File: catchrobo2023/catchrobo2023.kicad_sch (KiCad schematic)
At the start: 34 parts, among them J1 Conn_01x03_Male, J2 Conn_01x03_Male, J3 Conn_01x03_Male, J4 Conn_01x02_Male, J5 Conn_01x02_Male, J6 Conn_01x02_Male, J7 Conn_01x02_Male, J8 Conn_01x02_Male, Q1 AO3401A, SW1 SW_SPDT, SW2 SW_DIP_x04, U11 SPT15, U2 RaspberryPiPicoW, U3 AZ1084-5.0, U4 LBR-127HLD, U5 LBR-127HLD, U6 LBR-127HLD, U7 LBR-127HLD, U8 CD4051BM96

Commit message: 部品配置一旦終わり
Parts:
- U4, U5, U6, U7: footprint Connector_JST:JST_XH_B4B-XH-AM_1x04_P2.50mm_Vertical -> Connector_PinHeader_2.54mm:PinHeader_1x04_P2.54mm_Vertical
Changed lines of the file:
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@@
     (property "Reference" "U4" (id 0) (at 153.67 19.211 0))
     (property "Value" "LBR-127HLD" (id 1) (at 153.67 21.7479 0))
-    (property "Footprint" "Connector_JST:JST_XH_B4B-XH-AM_1x04_P2.50mm_Vertical" (id 2) (at 151.13 26.67 0)
+    (property "Footprint" "Connector_PinHeader_2.54mm:PinHeader_1x04_P2.54mm_Vertical" (id 2) (at 151.13 26.67 0)
       (effects (font (size 1.27 1.27)) hide)
     )
@@
     (property "Reference" "U7" (id 0) (at 153.67 80.171 0))
     (property "Value" "LBR-127HLD" (id 1) (at 153.67 82.7079 0))
-    (property "Footprint" "Connector_JST:JST_XH_B4B-XH-AM_1x04_P2.50mm_Vertical" (id 2) (at 151.13 87.63 0)
+    (property "Footprint" "Connector_PinHeader_2.54mm:PinHeader_1x04_P2.54mm_Vertical" (id 2) (at 151.13 87.63 0)
       (effects (font (size 1.27 1.27)) hide)
     )
@@
     (property "Reference" "U5" (id 0) (at 153.67 39.531 0))
     (property "Value" "LBR-127HLD" (id 1) (at 153.67 42.0679 0))
-    (property "Footprint" "Connector_JST:JST_XH_B4B-XH-AM_1x04_P2.50mm_Vertical" (id 2) (at 151.13 46.99 0)
+    (property "Footprint" "Connector_PinHeader_2.54mm:PinHeader_1x04_P2.54mm_Vertical" (id 2) (at 151.13 46.99 0)
       (effects (font (size 1.27 1.27)) hide)
     )
@@
     (property "Reference" "U6" (id 0) (at 153.67 59.851 0))
     (property "Value" "LBR-127HLD" (id 1) (at 153.67 62.3879 0))
-    (property "Footprint" "Connector_JST:JST_XH_B4B-XH-AM_1x04_P2.50mm_Vertical" (id 2) (at 151.13 67.31 0)
+    (property "Footprint" "Connector_PinHeader_2.54mm:PinHeader_1x04_P2.54mm_Vertical" (id 2) (at 151.13 67.31 0)
       (effects (font (size 1.27 1.27)) hide)
     )
@@
     )
     (path "/309bee41-de7c-4d48-85d7-c3c896b9413c"
-      (reference "U4") (unit 1) (value "LBR-127HLD") (footprint "Connector_JST:JST_XH_B4B-XH-AM_1x04_P2.50mm_Vertical")
+      (reference "U4") (unit 1) (value "LBR-127HLD") (footprint "Connector_PinHeader_2.54mm:PinHeader_1x04_P2.54mm_Vertical")
     )
     (path "/af13191f-f9fa-47db-8264-81b4e002b7be"
-      (reference "U5") (unit 1) (value "LBR-127HLD") (footprint "Connector_JST:JST_XH_B4B-XH-AM_1x04_P2.50mm_Vertical")
+      (reference "U5") (unit 1) (value "LBR-127HLD") (footprint "Connector_PinHeader_2.54mm:PinHeader_1x04_P2.54mm_Vertical")
     )
     (path "/c38467f7-e2c2-4708-991a-d2b698bca907"
-      (reference "U6") (unit 1) (value "LBR-127HLD") (footprint "Connector_JST:JST_XH_B4B-XH-AM_1x04_P2.50mm_Vertical")
+      (reference "U6") (unit 1) (value "LBR-127HLD") (footprint "Connector_PinHeader_2.54mm:PinHeader_1x04_P2.54mm_Vertical")
     )
     (path "/a7989e6a-60f8-412a-8d42-c272f1f8d212"
-      (reference "U7") (unit 1) (value "LBR-127HLD") (footprint "Connector_JST:JST_XH_B4B-XH-AM_1x04_P2.50mm_Vertical")
+      (reference "U7") (unit 1) (value "LBR-127HLD") (footprint "Connector_PinHeader_2.54mm:PinHeader_1x04_P2.54mm_Vertical")
     )
     (path "/319fb9ff-c20b-47c6-b5a0-e117048a4ec9"

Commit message: 部品配置完了！
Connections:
- net Sensor0: now also U8.15 (2); no longer U8.1 (4)
- net Sensor1: now also U8.14 (1); no longer U8.2 (6)
- net Sensor2: now also U8.13 (0); no longer U8.4 (7)
- net Sensor3: now also U8.12 (3); no longer U8.5 (8)
- net MultiC: no longer names the net of U8.9 (C)
- net MultiC: no longer U2.21 (GP16)
- no-connect marks 18 -> 20
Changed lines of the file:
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@@
   (no_connect (at 66.04 36.83))
   (no_connect (at 66.04 34.29))
-  (no_connect (at 165.1 106.68))
-  (no_connect (at 165.1 111.76))
-  (no_connect (at 165.1 109.22))
-  (no_connect (at 165.1 114.3))
   (no_connect (at 96.52 41.91))
   (no_connect (at 96.52 44.45))
   (no_connect (at 96.52 24.13))
+  (no_connect (at 96.52 69.85))
+  (no_connect (at 165.1 121.92))
+  (no_connect (at 147.32 114.3))
+  (no_connect (at 147.32 104.14))
+  (no_connect (at 147.32 106.68))
+  (no_connect (at 147.32 111.76))
   (no_connect (at 54.61 81.28))
   (no_connect (at 96.52 34.29))
@@
     (stroke (width 0) (type default) (color 0 0 0 0))
   )
-  (wire (pts (xy 165.1 121.92) (xy 168.91 121.92))
-    (stroke (width 0) (type default) (color 0 0 0 0))
-  )
   (wire (pts (xy 77.47 86.36) (xy 83.82 86.36))
     (stroke (width 0) (type default) (color 0 0 0 0))
@@
     (stroke (width 0) (type default) (color 0 0 0 0))
   )
-  (wire (pts (xy 143.51 104.14) (xy 147.32 104.14))
+  (wire (pts (xy 168.91 114.3) (xy 165.1 114.3))
     (stroke (width 0) (type default) (color 0 0 0 0))
   )
@@
     (stroke (width 0) (type default) (color 0 0 0 0))
   )
-  (wire (pts (xy 143.51 111.76) (xy 147.32 111.76))
+  (wire (pts (xy 168.91 109.22) (xy 165.1 109.22))
     (stroke (width 0) (type default) (color 0 0 0 0))
   )
@@
     (stroke (width 0) (type default) (color 0 0 0 0))
   )
-  (wire (pts (xy 96.52 69.85) (xy 101.6 69.85))
-    (stroke (width 0) (type default) (color 0 0 0 0))
-  )
   (wire (pts (xy 138.43 143.51) (xy 138.43 152.4))
     (stroke (width 0) (type default) (color 0 0 0 0))
@@
     (stroke (width 0) (type default) (color 0 0 0 0))
   )
-  (wire (pts (xy 143.51 106.68) (xy 147.32 106.68))
-    (stroke (width 0) (type default) (color 0 0 0 0))
-  )
-  (wire (pts (xy 143.51 114.3) (xy 147.32 114.3))
+  (wire (pts (xy 168.91 106.68) (xy 165.1 106.68))
+    (stroke (width 0) (type default) (color 0 0 0 0))
+  )
+  (wire (pts (xy 168.91 111.76) (xy 165.1 111.76))
     (stroke (width 0) (type default) (color 0 0 0 0))
   )
@@
     (effects (font (size 1.27 1.27)) (justify left bottom))
   )
-  (label "Sensor0" (at 143.51 104.14 180)
-    (effects (font (size 1.27 1.27)) (justify right bottom))
+  (label "Sensor3" (at 168.91 114.3 0)
+    (effects (font (size 1.27 1.27)) (justify left bottom))
   )
   (label "Servo2" (at 58.42 24.13 180)
     (effects (font (size 1.27 1.27)) (justify right bottom))
   )
-  (label "MultiC" (at 101.6 69.85 0)
-    (effects (font (size 1.27 1.27)) (justify left bottom))
-  )
   (label "DIPSW3" (at 104.14 54.61 0)
     (effects (font (size 1.27 1.27)) (justify left bottom))
   )
-  (label "Sensor3" (at 143.51 114.3 180)
-    (effects (font (size 1.27 1.27)) (justify right bottom))
+  (label "Sensor2" (at 168.91 111.76 0)
+    (effects (font (size 1.27 1.27)) (justify left bottom))
   )
   (label "Sensor2" (at 168.91 73.66 0)
     (effects (font (size 1.27 1.27)) (justify left bottom))
   )
-  (label "Sensor1" (at 143.51 106.68 180)
-    (effects (font (size 1.27 1.27)) (justify right bottom))
+  (label "Sensor0" (at 168.91 106.68 0)
+    (effects (font (size 1.27 1.27)) (justify left bottom))
   )
   (label "Servo2" (at 231.14 106.68 180)
@@
     (effects (font (size 1.27 1.27)) (justify right bottom))
   )
-  (label "Sensor2" (at 143.51 111.76 180)
-    (effects (font (size 1.27 1.27)) (justify right bottom))
+  (label "Sensor1" (at 168.91 109.22 0)
+    (effects (font (size 1.27 1.27)) (justify left bottom))
   )
   (label "DIPSW1" (at 78.74 146.05 0)
@@
     (effects (font (size 1.27 1.27)) (justify left bottom))
   )
-  (label "MultiC" (at 168.91 121.92 0)
-    (effects (font (size 1.27 1.27)) (justify left bottom))
-  )

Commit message: フォトリフレクタの周辺を修正
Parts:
- R10, R11, R2, R3, R4, R5: footprint Resistor_SMD:R_0201_0603Metric -> Resistor_SMD:R_0603_1608Metric
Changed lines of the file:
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@@
     (property "Reference" "R3" (id 0) (at 134.62 39.7342 90))
     (property "Value" "220" (id 1) (at 134.62 42.2711 90))
-    (property "Footprint" "Resistor_SMD:R_0201_0603Metric" (id 2) (at 134.62 46.228 90)
+    (property "Footprint" "Resistor_SMD:R_0603_1608Metric" (id 2) (at 134.62 46.228 90)
       (effects (font (size 1.27 1.27)) hide)
     )
@@
     (property "Reference" "R5" (id 0) (at 134.62 80.3742 90))
     (property "Value" "220" (id 1) (at 134.62 82.9111 90))
-    (property "Footprint" "Resistor_SMD:R_0201_0603Metric" (id 2) (at 134.62 86.868 90)
+    (property "Footprint" "Resistor_SMD:R_0603_1608Metric" (id 2) (at 134.62 86.868 90)
       (effects (font (size 1.27 1.27)) hide)
     )
@@
     (property "Reference" "R2" (id 0) (at 134.62 19.4142 90))
     (property "Value" "220" (id 1) (at 134.62 21.9511 90))
-    (property "Footprint" "Resistor_SMD:R_0201_0603Metric" (id 2) (at 134.62 25.908 90)
+    (property "Footprint" "Resistor_SMD:R_0603_1608Metric" (id 2) (at 134.62 25.908 90)
       (effects (font (size 1.27 1.27)) hide)
     )
@@
     (property "Reference" "R4" (id 0) (at 134.62 60.0542 90))
     (property "Value" "220" (id 1) (at 134.62 62.5911 90))
-    (property "Footprint" "Resistor_SMD:R_0201_0603Metric" (id 2) (at 134.62 66.548 90)
+    (property "Footprint" "Resistor_SMD:R_0603_1608Metric" (id 2) (at 134.62 66.548 90)
       (effects (font (size 1.27 1.27)) hide)
     )
@@
     (property "Reference" "R10" (id 0) (at 43.18 99.4242 90))
     (property "Value" "330" (id 1) (at 43.18 101.9611 90))
-    (property "Footprint" "Resistor_SMD:R_0201_0603Metric" (id 2) (at 43.18 105.918 90)
+    (property "Footprint" "Resistor_SMD:R_0603_1608Metric" (id 2) (at 43.18 105.918 90)
       (effects (font (size 1.27 1.27)) hide)
     )
@@
       (effects (font (size 1.27 1.27)) (justify left))
     )
-    (property "Footprint" "Resistor_SMD:R_0201_0603Metric" (id 2) (at 50.292 95.25 90)
+    (property "Footprint" "Resistor_SMD:R_0603_1608Metric" (id 2) (at 50.292 95.25 90)
       (effects (font (size 1.27 1.27)) hide)
     )
@@
     )
     (path "/4ece2eda-b20c-4e8f-ae6f-4d41de08f2b3"
-      (reference "R2") (unit 1) (value "220") (footprint "Resistor_SMD:R_0201_0603Metric")
+      (reference "R2") (unit 1) (value "220") (footprint "Resistor_SMD:R_0603_1608Metric")
     )
     (path "/485ce62a-bda4-46b8-b057-92a633eb73eb"
-      (reference "R3") (unit 1) (value "220") (footprint "Resistor_SMD:R_0201_0603Metric")
+      (reference "R3") (unit 1) (value "220") (footprint "Resistor_SMD:R_0603_1608Metric")
     )
     (path "/57897478-fc15-49af-a13c-0b635c80d981"
-      (reference "R4") (unit 1) (value "220") (footprint "Resistor_SMD:R_0201_0603Metric")
+      (reference "R4") (unit 1) (value "220") (footprint "Resistor_SMD:R_0603_1608Metric")
     )
     (path "/49080837-0b91-4e30-bf8a-b0058ad8b94b"
-      (reference "R5") (unit 1) (value "220") (footprint "Resistor_SMD:R_0201_0603Metric")
+      (reference "R5") (unit 1) (value "220") (footprint "Resistor_SMD:R_0603_1608Metric")
     )
     (path "/84754273-b66e-46a4-8959-627db908f4ff"
@@
     )
     (path "/5c226758-3cc0-45c8-83c2-343691c8c69e"
-      (reference "R10") (unit 1) (value "330") (footprint "Resistor_SMD:R_0201_0603Metric")
+      (reference "R10") (unit 1) (value "330") (footprint "Resistor_SMD:R_0603_1608Metric")
     )
     (path "/e09fb322-eccd-41fe-9289-f843fa181def"
-      (reference "R11") (unit 1) (value "10k") (footprint "Resistor_SMD:R_0201_0603Metric")
+      (reference "R11") (unit 1) (value "10k") (footprint "Resistor_SMD:R_0603_1608Metric")
     )
     (path "/f8c78e15-c342-4ab0-8f4b-67d61e7bd8ef"

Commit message: 製造ファイルまで出力
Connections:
- net Sensor0: now also U8.13 (0); no longer U8.15 (2)
- net Sensor2: now also U8.15 (2); no longer U8.13 (0)
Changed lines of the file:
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@@
     (effects (font (size 1.27 1.27)) (justify left bottom))
   )
-  (label "Sensor2" (at 168.91 111.76 0)
+  (label "Sensor0" (at 168.91 111.76 0)
     (effects (font (size 1.27 1.27)) (justify left bottom))
   )
@@
     (effects (font (size 1.27 1.27)) (justify left bottom))
   )
-  (label "Sensor0" (at 168.91 106.68 0)
+  (label "Sensor2" (at 168.91 106.68 0)
     (effects (font (size 1.27 1.27)) (justify left bottom))
   )

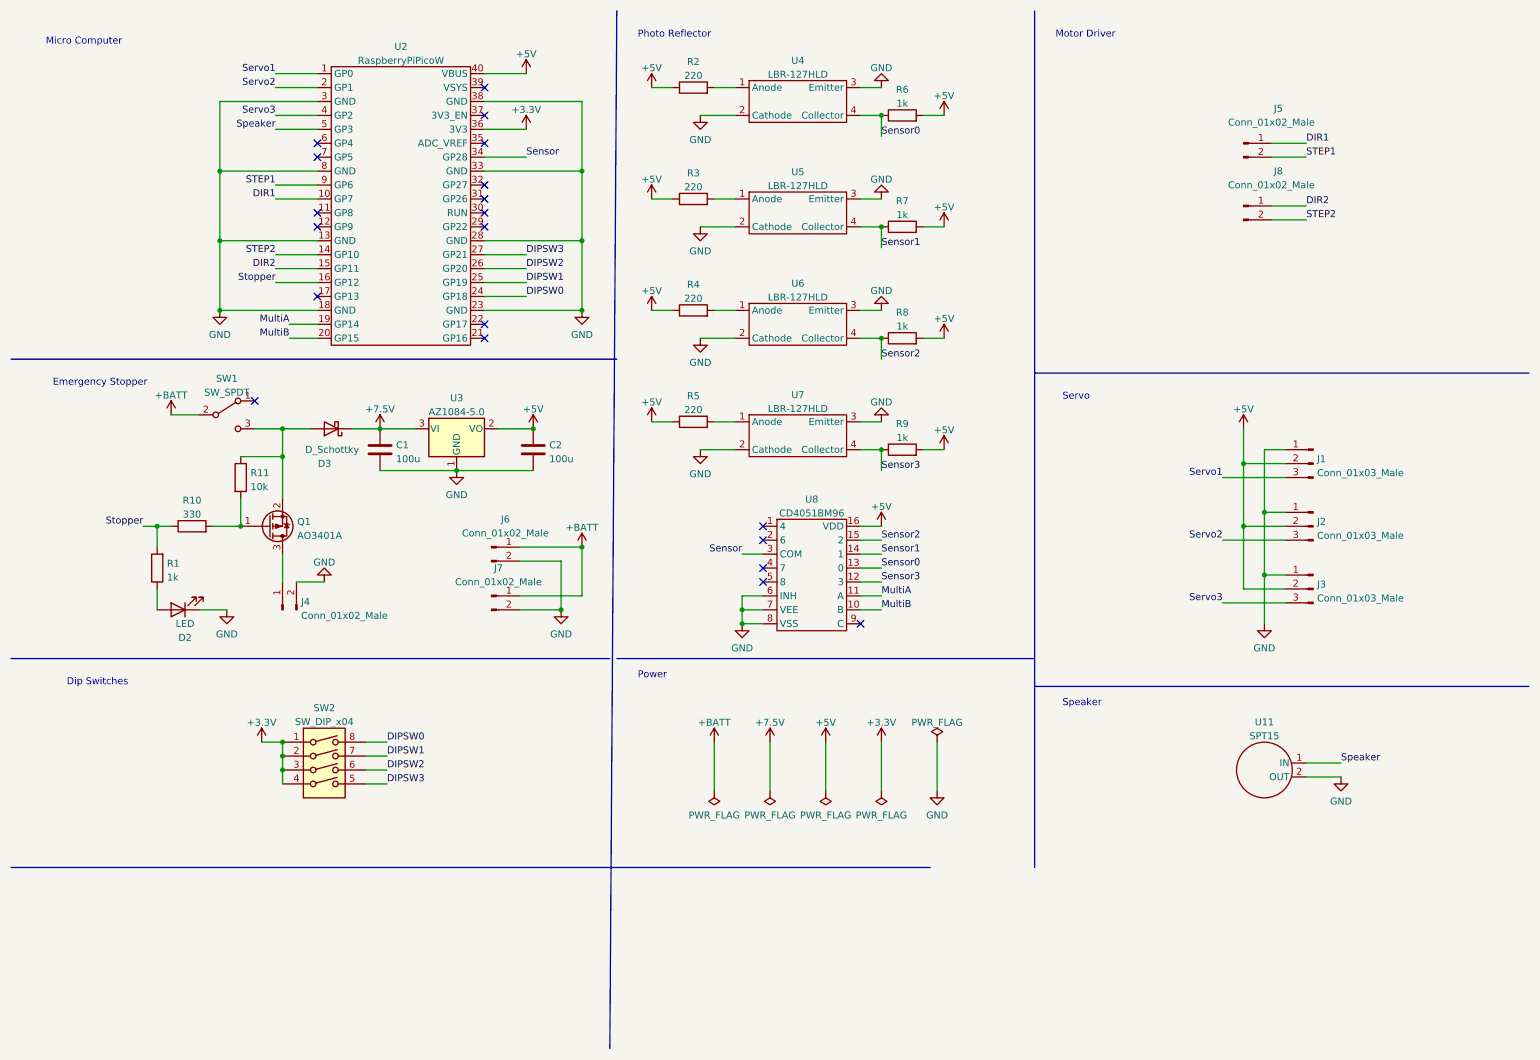
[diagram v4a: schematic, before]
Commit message: 5V電源(XH)を追加
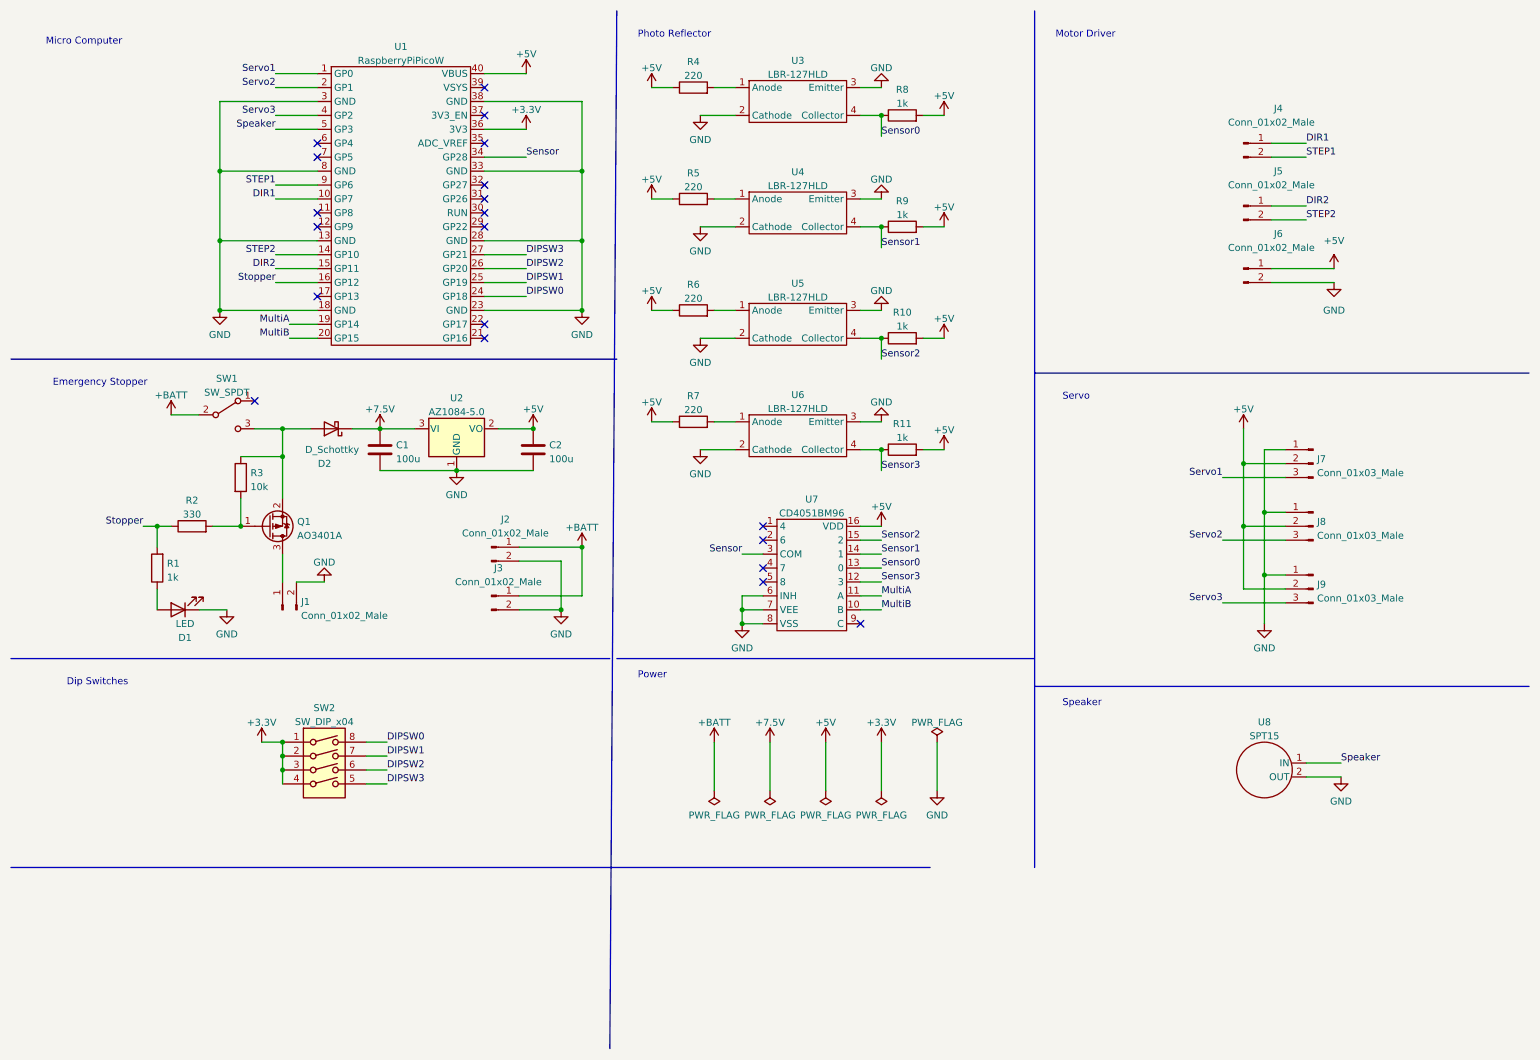
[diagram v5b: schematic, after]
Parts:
- added J6: Conn_01x02_Male, Connector_JST:JST_XH_B2B-XH-AM_1x02_P2.50mm_Vertical, symbol Connector:Conn_01x02_Male
- renumbered D2 to D1, D3 to D2, J4 to J1, J6 to J2, J7 to J3, J5 to J4, J8 to J5, J1 to J7, J2 to J8, J3 to J9, R8 to R10, R9 to R11, R10 to R2, R11 to R3, R2 to R4, R3 to R5, R4 to R6, R5 to R7, R6 to R8, R7 to R9, U2 to U1, U3 to U2, U4 to U3, U5 to U4, U6 to U5, U7 to U6, U8 to U7, U11 to U8
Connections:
- net +5V: now also J6.1 (Pin_1)
- net GND: now also J6.2 (Pin_2)
